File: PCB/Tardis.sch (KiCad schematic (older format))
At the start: 54 parts, among them Q1 2N3904, U1 RDC2072S12, U2 L4940, U3 MT8888C, U4 MT8888C, Y1 3.579545MHz, Y2 3.579545MHz

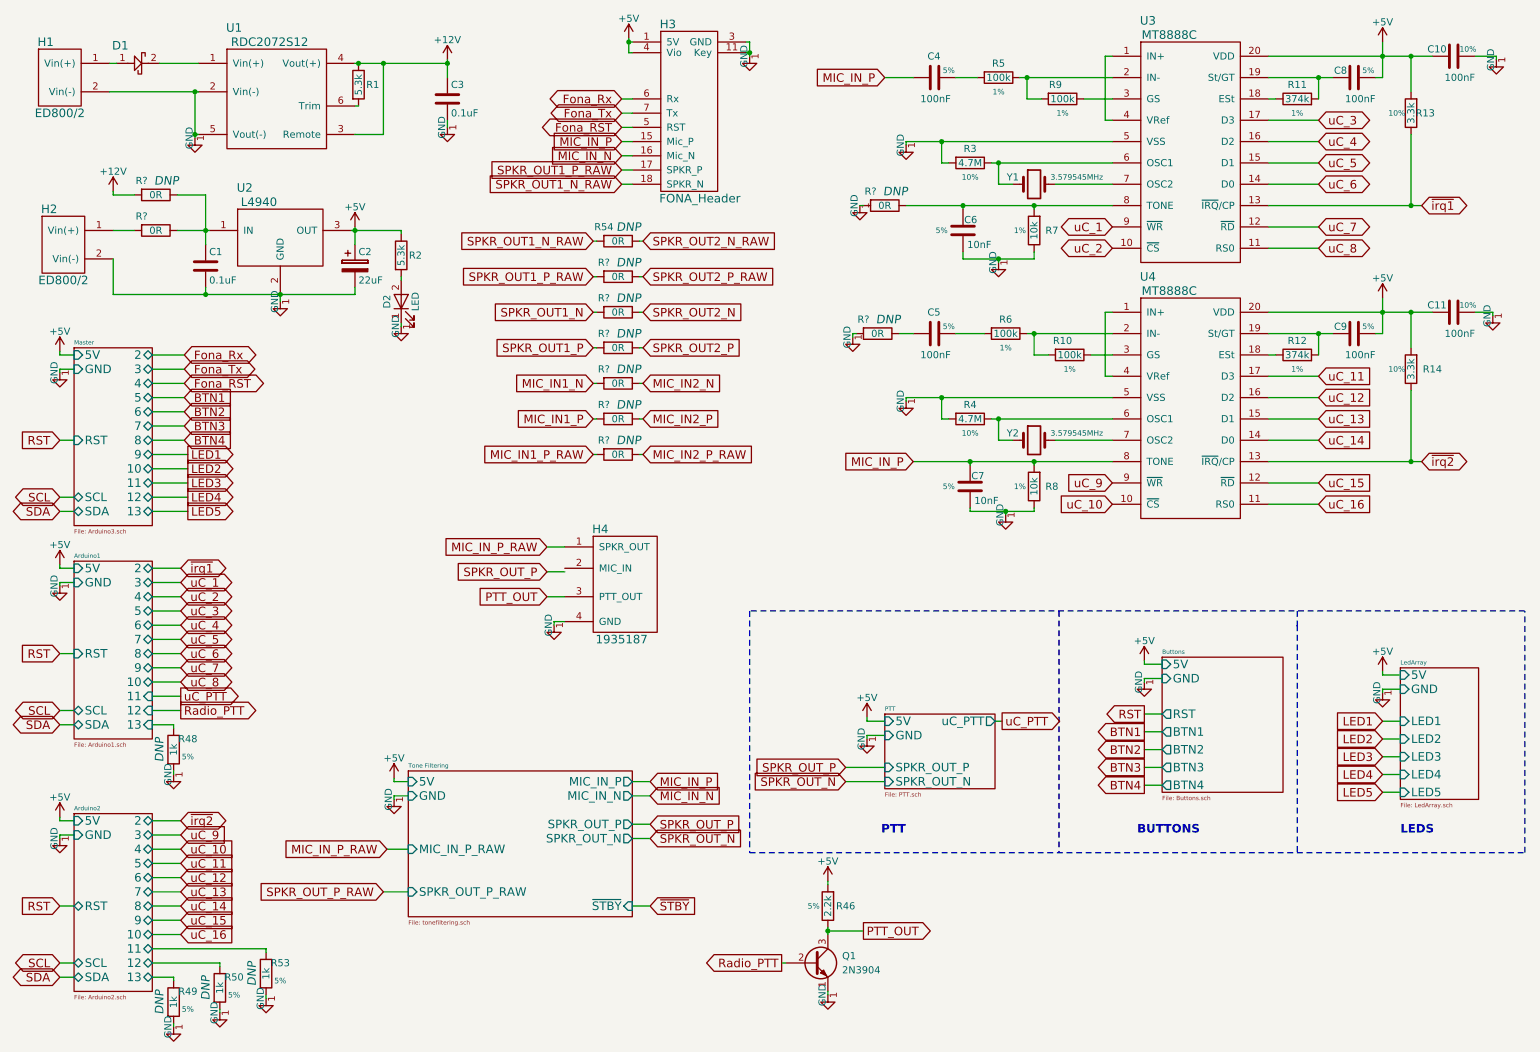
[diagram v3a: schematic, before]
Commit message: Added PCB layout
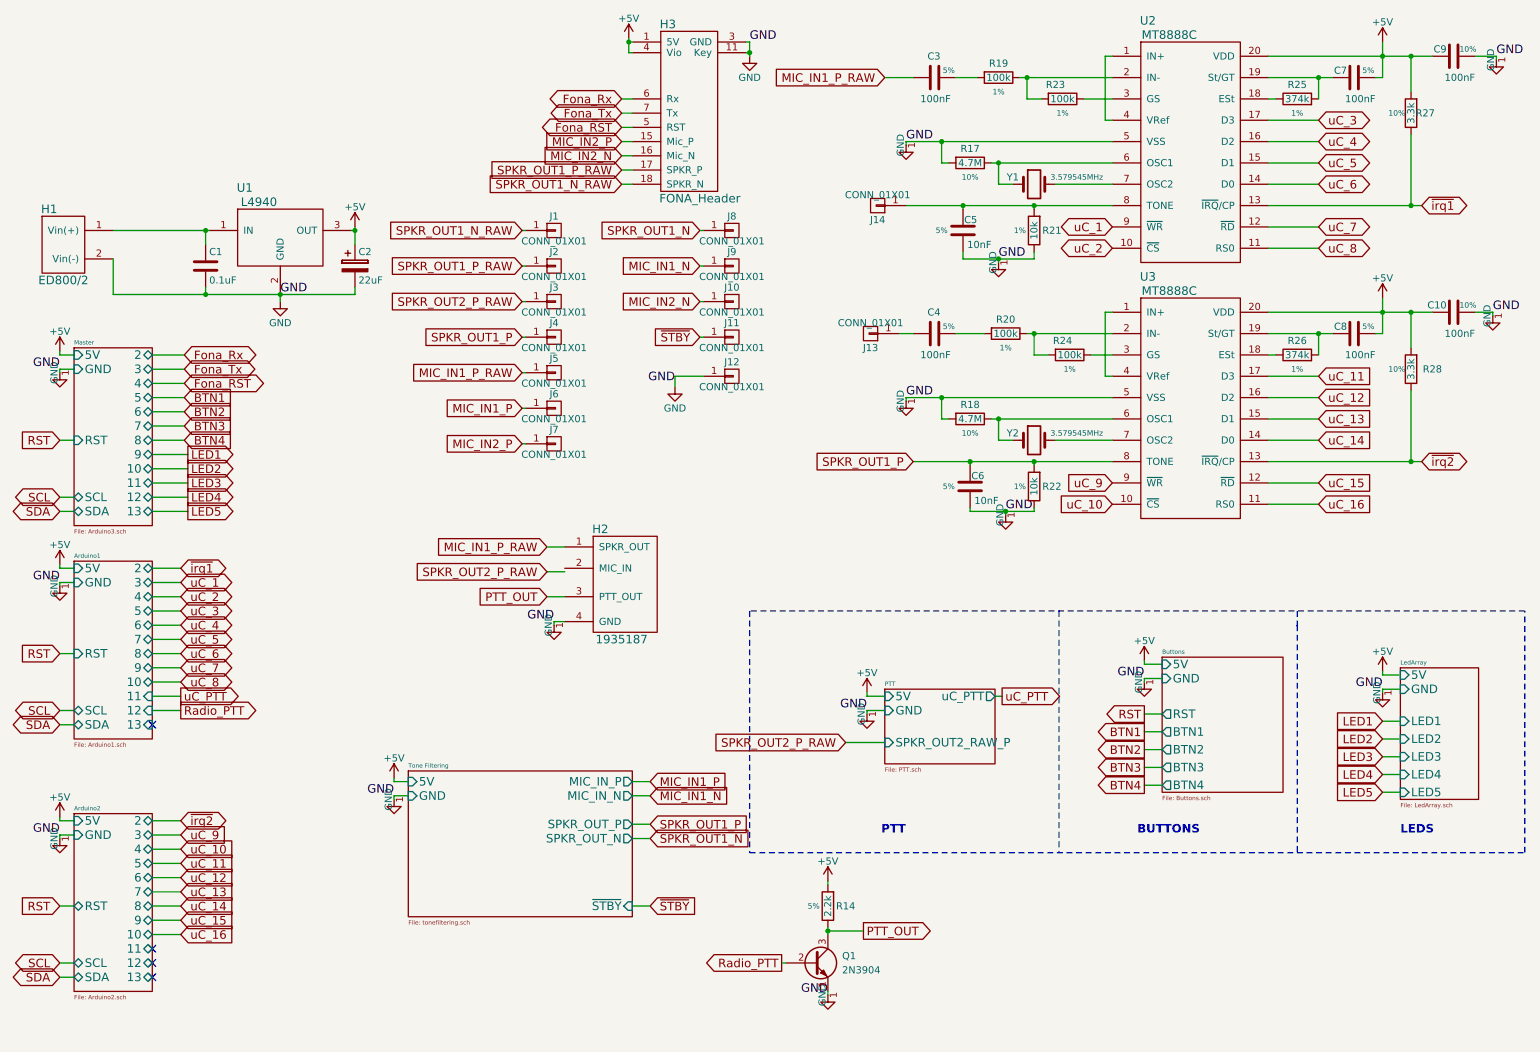
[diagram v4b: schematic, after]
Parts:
- removed C3: 0.1uF, Footprints:1206, symbol C
- removed D1: diode, symbol diode
- removed D2: LED, symbol LED
- removed H1: ED800/2, Footprints:ED800-2, symbol ED800
- removed R1, R2: 5.3k, symbol R
- removed R48, R49, R50, R53: 1k, symbol R
- removed R54, R? (x10): 0R, Resistor_THT:R_Axial_DIN0207_L6.3mm_D2.5mm_P2.54mm_Vertical, symbol R
- removed U1: RDC2072S12, Footprints:RDC2072S12, symbol RDC2072S12
- added J1, J10, J11, J12, J13, J14, J2, J3, J4, J5, J6, J7, J8, J9: CONN_01X01, Pin_Headers:Pin_Header_Straight_1x01_Pitch2.54mm, symbol CONN_01X01
- C1: footprint Footprints:1206 -> Capacitors_SMD:C_0603_HandSoldering
- C10: renamed from C11; footprint Footprints:1206 -> Capacitors_SMD:C_0603_HandSoldering
- C3: renamed from C4; footprint Footprints:1206 -> Capacitors_SMD:C_0603_HandSoldering
- C4: renamed from C5; footprint Footprints:1206 -> Capacitors_SMD:C_0603_HandSoldering
- C5: renamed from C6; footprint Footprints:1206 -> Capacitors_SMD:C_0603_HandSoldering
- C6: renamed from C7; footprint Footprints:1206 -> Capacitors_SMD:C_0603_HandSoldering
- C7: renamed from C8; footprint Footprints:1206 -> Capacitors_SMD:C_0603_HandSoldering
- C8: renamed from C9; footprint Footprints:1206 -> Capacitors_SMD:C_0603_HandSoldering
- C9: renamed from C10; footprint Footprints:1206 -> Capacitors_SMD:C_0603_HandSoldering
- H1: renamed from H2; footprint Footprints:ED800-2 -> Footprints:ED800
- Q1: footprint (none) -> TO_SOT_Packages_THT:TO-92_Molded_Narrow
- R14: renamed from R46; footprint (none) -> Resistors_SMD:R_0603_HandSoldering
- R17: renamed from R3; footprint (none) -> Resistors_SMD:R_0603_HandSoldering
- R18: renamed from R4; footprint (none) -> Resistors_SMD:R_0603_HandSoldering
- R19: renamed from R5; footprint (none) -> Resistors_SMD:R_0603_HandSoldering
- R20: renamed from R6; footprint (none) -> Resistors_SMD:R_0603_HandSoldering
- R21: renamed from R7; footprint (none) -> Resistors_SMD:R_0603_HandSoldering
- R22: renamed from R8; footprint (none) -> Resistors_SMD:R_0603_HandSoldering
- R23: renamed from R9; footprint (none) -> Resistors_SMD:R_0603_HandSoldering
- R24: renamed from R10; footprint (none) -> Resistors_SMD:R_0603_HandSoldering
- R25: renamed from R11; footprint (none) -> Resistors_SMD:R_0603_HandSoldering
- R26: renamed from R12; footprint (none) -> Resistors_SMD:R_0603_HandSoldering
- R27: renamed from R13; footprint (none) -> Resistors_SMD:R_0603_HandSoldering
- R28: renamed from R14; footprint (none) -> Resistors_SMD:R_0603_HandSoldering
- U1: renamed from U2; footprint TO_SOT_Packages_THT:TO-220-3_Vertical -> TO_SOT_Packages_THT:TO-220-3_Horizontal
- Y1, Y2: footprint (none) -> Crystals:Crystal_SMD_HC49-SD_HandSoldering
- renumbered H4 to H2, U3 to U2, U4 to U3
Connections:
- net MIC_IN_N is gone; now on net MIC_IN2_N: H3.16 (Mic_N)
- net MIC_IN_P_RAW is gone; now on net MIC_IN1_P_RAW: H2.1 (SPKR_OUT)
- net MIC_IN1_N: now also J9.1 (P1)
- net MIC_IN1_P: now also J6.1 (P1)
- net MIC_IN1_P_RAW: now also C3.2, J5.1 (P1)
- net MIC_IN2_N: now also J10.1 (P1)
- net MIC_IN2_P: now also H3.15 (Mic_P), J7.1 (P1)
- net SPKR_OUT1_N: now also J8.1 (P1)
- net SPKR_OUT1_N_RAW: now also J1.1 (P1)
- net SPKR_OUT1_P: now also C6.2, R22.2, U3.8 (TONE), J4.1 (P1)
- net SPKR_OUT1_P_RAW: now also J2.1 (P1)
- net SPKR_OUT2_P_RAW: now also J3.1 (P1)
- net ~STBY: now also J11.1 (P1)
- net at H1.1 (Vin(+)): now also C1.1, U1.1 (IN)
- net GND: now reaches C1.2, C2.2, H1.2 (Vin(-)), U1.2 (GND)
- net GND: now also C10.2, C5.1, C6.1, C9.2, H2.4 (GND), H3.11 (Key), H3.3 (GND), Q1.1 (E), R17.2, R18.2, R21.1, R22.1, U2.5 (VSS), U3.5 (VSS), J12.1 (P1)
- net at C5.2, R21.2, U2.8 (TONE): now also J14.1 (P1)
- net at C4.2: now also J13.1 (P1)
- removed net MIC_IN_P: C3.2, C6.2, H3.15 (Mic_P), R22.2, U3.8 (TONE)
- no-connect marks 0 -> 4

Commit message: PCB Done. To be reviewed.
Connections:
- net MIC_IN1_P_RAW: now also H2.2 (MIC_IN); no longer H2.1 (SPKR_OUT)
- net SPKR_OUT2_P_RAW: now also H2.1 (SPKR_OUT)
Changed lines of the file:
@@
 Wire Wire Line
 	4800 1350 4875 1350
-Text GLabel 1725 2950 2    60   BiDi ~ 0
+Text GLabel 1725 3150 2    60   BiDi ~ 0
 Fona_Rx
 Text GLabel 1725 3050 2    60   BiDi ~ 0
 Fona_Tx
-Text GLabel 1725 3150 2    60   BiDi ~ 0
+Text GLabel 1725 2950 2    60   BiDi ~ 0
 Fona_RST
 Wire Wire Line
@@
 Text GLabel 4800 1650 0    60   Input ~ 0
 SPKR_OUT1_P_RAW
-Text GLabel 4275 4300 0    60   Input ~ 0
+Text GLabel 4275 4450 0    60   Input ~ 0
 MIC_IN1_P_RAW
 Text GLabel 5000 5950 2    60   Input ~ 0
@@
 Wire Wire Line
 	4875 6350 5000 6350
-Text GLabel 4275 4475 0    60   Input ~ 0
+Text GLabel 4275 4300 0    60   Input ~ 0
 SPKR_OUT2_P_RAW
 Wire Wire Line
 	4850 750  4875 750
 $Comp
-L +5V #PWR12
+L +5V #PWR01
 U 1 1 5A2B0D81
 P 4850 725
-F 0 "#PWR12" H 4850 575 50  0001 C CNN
+F 0 "#PWR01" H 4850 575 50  0001 C CNN
 F 1 "+5V" H 4850 865 50  0000 C CNN
 F 2 "" H 4850 725 50  0001 C CNN
@@
 $EndComp
 $Comp
-L +5V #PWR8
+L +5V #PWR02
 U 1 1 5A2B1432
 P 2925 2050
-F 0 "#PWR8" H 2925 1900 50  0001 C CNN
+F 0 "#PWR02" H 2925 1900 50  0001 C CNN
 F 1 "+5V" H 2925 2190 50  0000 C CNN
 F 2 "" H 2925 2050 50  0001 C CNN
@@
 $EndComp
 $Comp
-L +5V #PWR1
+L +5V #PWR03
 U 1 1 5A2B445E
 P 850 2925
-F 0 "#PWR1" H 850 2775 50  0001 C CNN
+F 0 "#PWR03" H 850 2775 50  0001 C CNN
 F 1 "+5V" H 850 3065 50  0000 C CNN
 F 2 "" H 850 2925 50  0001 C CNN
@@
 $EndComp
 $Comp
-L +5V #PWR3
+L +5V #PWR04
 U 1 1 5A2B5128
 P 850 4425
-F 0 "#PWR3" H 850 4275 50  0001 C CNN
+F 0 "#PWR04" H 850 4275 50  0001 C CNN
 F 1 "+5V" H 850 4565 50  0000 C CNN
 F 2 "" H 850 4425 50  0001 C CNN
@@
 $EndComp
 $Comp
-L +5V #PWR5
+L +5V #PWR05
 U 1 1 5A2B6440
 P 850 6200
-F 0 "#PWR5" H 850 6050 50  0001 C CNN
+F 0 "#PWR05" H 850 6050 50  0001 C CNN
 F 1 "+5V" H 850 6340 50  0000 C CNN
 F 2 "" H 850 6200 50  0001 C CNN
@@
 $EndComp
 $Comp
-L +5V #PWR17
+L +5V #PWR06
 U 1 1 5A2B712D
 P 6525 5325
-F 0 "#PWR17" H 6525 5175 50  0001 C CNN
+F 0 "#PWR06" H 6525 5175 50  0001 C CNN
 F 1 "+5V" H 6525 5465 50  0000 C CNN
 F 2 "" H 6525 5325 50  0001 C CNN
@@
 $EndComp
 $Comp
-L +5V #PWR23
+L +5V #PWR07
 U 1 1 5A2B77A9
 P 8475 5100
-F 0 "#PWR23" H 8475 4950 50  0001 C CNN
+F 0 "#PWR07" H 8475 4950 50  0001 C CNN
 F 1 "+5V" H 8475 5240 50  0000 C CNN
 F 2 "" H 8475 5100 50  0001 C CNN
@@
 $EndComp
 $Comp
-L +5V #PWR27
+L +5V #PWR08
 U 1 1 5A2B79F1
 P 10150 5175
-F 0 "#PWR27" H 10150 5025 50  0001 C CNN
+F 0 "#PWR08" H 10150 5025 50  0001 C CNN
 F 1 "+5V" H 10150 5315 50  0000 C CNN
 F 2 "" H 10150 5175 50  0001 C CNN
@@
 $EndComp
 $Comp
-L +5V #PWR26
+L +5V #PWR09
 U 1 1 5A2B913D
 P 10150 2550
-F 0 "#PWR26" H 10150 2400 50  0001 C CNN
+F 0 "#PWR09" H 10150 2400 50  0001 C CNN
 F 1 "+5V" H 10150 2690 50  0000 C CNN
 F 2 "" H 10150 2550 50  0001 C CNN
@@
 $EndComp
 $Comp
-L +5V #PWR25
+L +5V #PWR010
 U 1 1 5A2B93A8
 P 10150 750
-F 0 "#PWR25" H 10150 600 50  0001 C CNN
+F 0 "#PWR010" H 10150 600 50  0001 C CNN
 F 1 "+5V" H 10150 890 50  0000 C CNN
 F 2 "" H 10150 750 50  0001 C CNN
@@
 $EndComp
 $Comp
-L GND-RESCUE-Tardis #PWR2
+L GND-RESCUE-Tardis #PWR011
 U 1 1 5A2C3E5D
 P 850 3075
-F 0 "#PWR2" H 850 2825 50  0001 C CNN
+F 0 "#PWR011" H 850 2825 50  0001 C CNN
 F 1 "GND" H 850 2925 50  0001 C CNN
 F 2 "" H 850 3075 50  0001 C CNN
@@
 $EndComp
 $Comp
-L GND-RESCUE-Tardis #PWR4
+L GND-RESCUE-Tardis #PWR012
 U 1 1 5A2C6F69
 P 850 4575
-F 0 "#PWR4" H 850 4325 50  0001 C CNN
+F 0 "#PWR012" H 850 4325 50  0001 C CNN
 F 1 "GND" H 850 4425 50  0001 C CNN
 F 2 "" H 850 4575 50  0001 C CNN
@@
 	850  4575 850  4550
 $Comp
-L GND-RESCUE-Tardis #PWR6
+L GND-RESCUE-Tardis #PWR013
 U 1 1 5A2DE68C
 P 850 6350
-F 0 "#PWR6" H 850 6100 50  0001 C CNN
+F 0 "#PWR013" H 850 6100 50  0001 C CNN
 F 1 "GND" H 850 6200 50  0001 C CNN
 F 2 "" H 850 6350 50  0001 C CNN
@@
 	850  6325 950  6325
 $Comp
-L GND-RESCUE-Tardis #PWR18
+L GND-RESCUE-Tardis #PWR014
 U 1 1 5A2E2BFF
 P 6525 5475
-F 0 "#PWR18" H 6525 5225 50  0001 C CNN
+F 0 "#PWR014" H 6525 5225 50  0001 C CNN
 F 1 "GND" H 6525 5325 50  0001 C CNN
 F 2 "" H 6525 5475 50  0001 C CNN
@@
 $EndComp
 $Comp
-L GND-RESCUE-Tardis #PWR24
+L GND-RESCUE-Tardis #PWR015
 U 1 1 5A2E316E
 P 8475 5250
-F 0 "#PWR24" H 8475 5000 50  0001 C CNN
+F 0 "#PWR015" H 8475 5000 50  0001 C CNN
 F 1 "GND" H 8475 5100 50  0001 C CNN
 F 2 "" H 8475 5250 50  0001 C CNN
@@
 $EndComp
 $Comp
-L GND-RESCUE-Tardis #PWR28
+L GND-RESCUE-Tardis #PWR016
 U 1 1 5A2E33B6
 P 10150 5325
-F 0 "#PWR28" H 10150 5075 50  0001 C CNN
+F 0 "#PWR016" H 10150 5075 50  0001 C CNN
 F 1 "GND" H 10150 5175 50  0001 C CNN
 F 2 "" H 10150 5325 50  0001 C CNN
@@
 	10150 5200 10275 5200
 $Comp
-L GND-RESCUE-Tardis #PWR22
+L GND-RESCUE-Tardis #PWR017
 U 1 1 5A2F48FD
 P 7500 4075
-F 0 "#PWR22" H 7500 3825 50  0001 C CNN
+F 0 "#PWR017" H 7500 3825 50  0001 C CNN
 F 1 "GND" H 7500 3925 50  0001 C CNN
 F 2 "" H 7500 4075 50  0001 C CNN
@@
 $EndComp
 $Comp
-L GND-RESCUE-Tardis #PWR20
+L GND-RESCUE-Tardis #PWR018
 U 1 1 5A2F93C3
 P 6800 3275
-F 0 "#PWR20" H 6800 3025 50  0001 C CNN
+F 0 "#PWR018" H 6800 3025 50  0001 C CNN
 F 1 "GND" H 6800 3125 50  0001 C CNN
 F 2 "" H 6800 3275 50  0001 C CNN
@@
 	6800 3275 6800 3250
 $Comp
-L GND-RESCUE-Tardis #PWR29
+L GND-RESCUE-Tardis #PWR019
 U 1 1 5A3025FE
 P 10925 2675
-F 0 "#PWR29" H 10925 2425 50  0001 C CNN
+F 0 "#PWR019" H 10925 2425 50  0001 C CNN
 F 1 "GND" H 10925 2525 50  0001 C CNN
 F 2 "" H 10925 2675 50  0001 C CNN
@@
 	10925 2650 10925 2675
 $Comp
-L GND-RESCUE-Tardis #PWR30
+L GND-RESCUE-Tardis #PWR020
 U 1 1 5A30A76A
 P 10950 875
-F 0 "#PWR30" H 10950 625 50  0001 C CNN
+F 0 "#PWR020" H 10950 625 50  0001 C CNN
 F 1 "GND" H 10950 725 50  0001 C CNN
 F 2 "" H 10950 875 50  0001 C CNN
@@
 	10950 875  10950 850
 $Comp
-L GND-RESCUE-Tardis #PWR19
+L GND-RESCUE-Tardis #PWR021
 U 1 1 5A30E597
 P 6800 1475
-F 0 "#PWR19" H 6800 1225 50  0001 C CNN
+F 0 "#PWR021" H 6800 1225 50  0001 C CNN
 F 1 "GND" H 6800 1325 50  0001 C CNN
 F 2 "" H 6800 1475 50  0001 C CNN
@@
 $EndComp
 $Comp
-L GND-RESCUE-Tardis #PWR21
+L GND-RESCUE-Tardis #PWR022
 U 1 1 5A3126EB
 P 7450 2300
-F 0 "#PWR21" H 7450 2050 50  0001 C CNN
+F 0 "#PWR022" H 7450 2050 50  0001 C CNN
 F 1 "GND" H 7450 2150 50  0001 C CNN
 F 2 "" H 7450 2300 50  0001 C CNN
@@
 	6525 5450 6650 5450
 $Comp
-L +5V #PWR9
+L +5V #PWR023
 U 1 1 5A3667F5
 P 3200 5925
-F 0 "#PWR9" H 3200 5775 50  0001 C CNN
+F 0 "#PWR023" H 3200 5775 50  0001 C CNN
 F 1 "+5V" H 3200 6065 50  0000 C CNN
 F 2 "" H 3200 5925 50  0001 C CNN
@@
 $EndComp
 $Comp
-L GND-RESCUE-Tardis #PWR10
+L GND-RESCUE-Tardis #PWR024
 U 1 1 5A3667FB
 P 3200 6075
-F 0 "#PWR10" H 3200 5825 50  0001 C CNN
+F 0 "#PWR024" H 3200 5825 50  0001 C CNN
 F 1 "GND" H 3200 5925 50  0001 C CNN
 F 2 "" H 3200 6075 50  0001 C CNN
@@
 PTT_OUT
 $Comp
-L GND-RESCUE-Tardis #PWR11
+L GND-RESCUE-Tardis #PWR025
 U 1 1 5A255D6A
 P 4325 4850
-F 0 "#PWR11" H 4325 4600 50  0001 C CNN
+F 0 "#PWR025" H 4325 4600 50  0001 C CNN
 F 1 "GND" H 4325 4700 50  0001 C CNN
 F 2 "" H 4325 4850 50  0001 C CNN
@@
 Radio_PTT
 $Comp
-L GND-RESCUE-Tardis #PWR16
+L GND-RESCUE-Tardis #PWR026
 U 1 1 5A2689C9
 P 6250 7450
-F 0 "#PWR16" H 6250 7200 50  0001 C CNN
+F 0 "#PWR026" H 6250 7200 50  0001 C CNN
 F 1 "GND" H 6250 7300 50  0001 C CNN
 F 2 "" H 6250 7450 50  0001 C CNN
@@
 $EndComp
 $Comp
-L +5V #PWR15
+L +5V #PWR027
 U 1 1 5A268E8A
 P 6250 6650
-F 0 "#PWR15" H 6250 6500 50  0001 C CNN
+F 0 "#PWR027" H 6250 6500 50  0001 C CNN
 F 1 "+5V" H 6250 6790 50  0000 C CNN
 F 2 "" H 6250 6650 50  0001 C CNN
@@
 	6650 5675 6375 5675
 $Comp
-L GND #PWR7
+L GND #PWR028
 U 1 1 5A58EB77
 P 2400 2575
-F 0 "#PWR7" H 2400 2325 50  0001 C CNN
+F 0 "#PWR028" H 2400 2325 50  0001 C CNN
 F 1 "GND" H 2400 2425 50  0000 C CNN
 F 2 "" H 2400 2575 50  0001 C CNN
@@
 $EndComp
 $Comp
-L GND #PWR14
+L GND #PWR029
 U 1 1 5A49AB0B
 P 5700 850
-F 0 "#PWR14" H 5700 600 50  0001 C CNN
+F 0 "#PWR029" H 5700 600 50  0001 C CNN
 F 1 "GND" H 5700 700 50  0000 C CNN
 F 2 "" H 5700 850 50  0001 C CNN
@@
 	1    0    0    -1
 $EndComp
-Wire Wire Line
-	4400 4475 4275 4475
 Text GLabel 6650 1000 0    60   Input ~ 0
 MIC_IN1_P_RAW
 $Comp
-L GND #PWR13
+L GND #PWR030
 U 1 1 5A4C46CA
 P 5175 3175
-F 0 "#PWR13" H 5175 2925 50  0001 C CNN
+F 0 "#PWR030" H 5175 2925 50  0001 C CNN
 F 1 "GND" H 5175 3025 50  0000 C CNN
 F 2 "" H 5175 3175 50  0001 C CNN
@@
 	-1   0    0    1
 $EndComp
+Wire Wire Line
+	4400 4450 4275 4450
 $EndSCHEMATC
